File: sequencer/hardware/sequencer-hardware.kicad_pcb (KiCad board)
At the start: 4 copper layers, 111 parts, among them J1 Barrel Jack, J10 JST_4-pin_male, J11 Conn_01x03, J12 Conn_01x03, J13 Conn_01x03, J14 Conn_01x03, J15 JST_4-pin_male, J16 JST_4-pin_male, J17 Conn_01x03, J2 40Pin 0.1", J3 USB_B_Micro, J4 Conn_01x02_Male, J5 JST 4-Pin male, J6 TS Out, J7 Conn_01x03_Male, J8 Conn_01x03_Male, J9 JST_4-pin_male, SW2 SW_Push, SW3 SW_Push, U1 L7805_A, U2 L7805_D, U3 ICL7660, U4 NCP1117-3.3_TO252, U5 OPA703UA, U6 OPA703UA, U7 W25Q128JVS, U8 RP2040, Y1 12MHz 18pF

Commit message: More routing
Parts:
- moved R2 150.9 mm to (57.1, 135.5), turned to -90 degrees
- moved SW2 148.6 mm to (63.5, 133.3)
- moved R24 138.5 mm to (238.3, 24.1), turned to 0 degrees
- moved J10 130.8 mm to (222.2, 19.1), turned to -90 degrees
- moved R23 130.6 mm to (238.3, 20.3), turned to 0 degrees
- moved R1 129.1 mm to (76.6, 109.2)
- moved R22 127.7 mm to (232.8, 24.1), turned to 0 degrees
- moved R16 127.6 mm to (231.1, 130.4), turned to -90 degrees
- moved C20 122.5 mm to (228.6, 141.0), turned to 90 degrees
- moved R28 121.3 mm to (252.2, 60.5)
- moved R15 119.8 mm to (231.1, 117.7), turned to -90 degrees
- moved C22 119.5 mm to (231.1, 141.0), turned to 90 degrees
- moved R27 118.4 mm to (252.2, 65.2)
- moved C24 117.7 mm to (234.9, 140.6), turned to 90 degrees
- moved C26 116.3 mm to (237.5, 140.6), turned to 90 degrees
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
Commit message: Adjust component placement
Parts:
- added SW1: PWR, Connector_PinHeader_2.00mm:PinHeader_1x02_P2.00mm_Vertical, F.Cu at (49.9, 44.7)
- moved C28 186.6 mm to (76.7, 112.0)
- moved C29 186.6 mm to (76.7, 117.1)
- moved R27 186.6 mm to (72.9, 116.9)
- moved R29 186.6 mm to (69.1, 112.1)
- moved R30 186.6 mm to (69.1, 116.9)
- moved R28 179.5 mm to (78.0, 103.6)
- moved J15 176.0 mm to (71.8, 105.1)
- moved J17 168.3 mm to (64.4, 62.7), turned to -90 degrees
- moved R33 161.4 mm to (67.8, 81.0), turned to -90 degrees
- moved R23 160.6 mm to (83.4, 62.6), turned to 180 degrees
- moved C37 158.8 mm to (70.1, 145.8), turned to 90 degrees
- moved C36 158.7 mm to (72.6, 145.8), turned to 90 degrees
- moved C35 158.6 mm to (75.2, 145.8), turned to 90 degrees
- moved R34 158.1 mm to (68.6, 75.2), turned to -90 degrees
- moved R24 154.8 mm to (88.6, 63.5), turned to 180 degrees
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
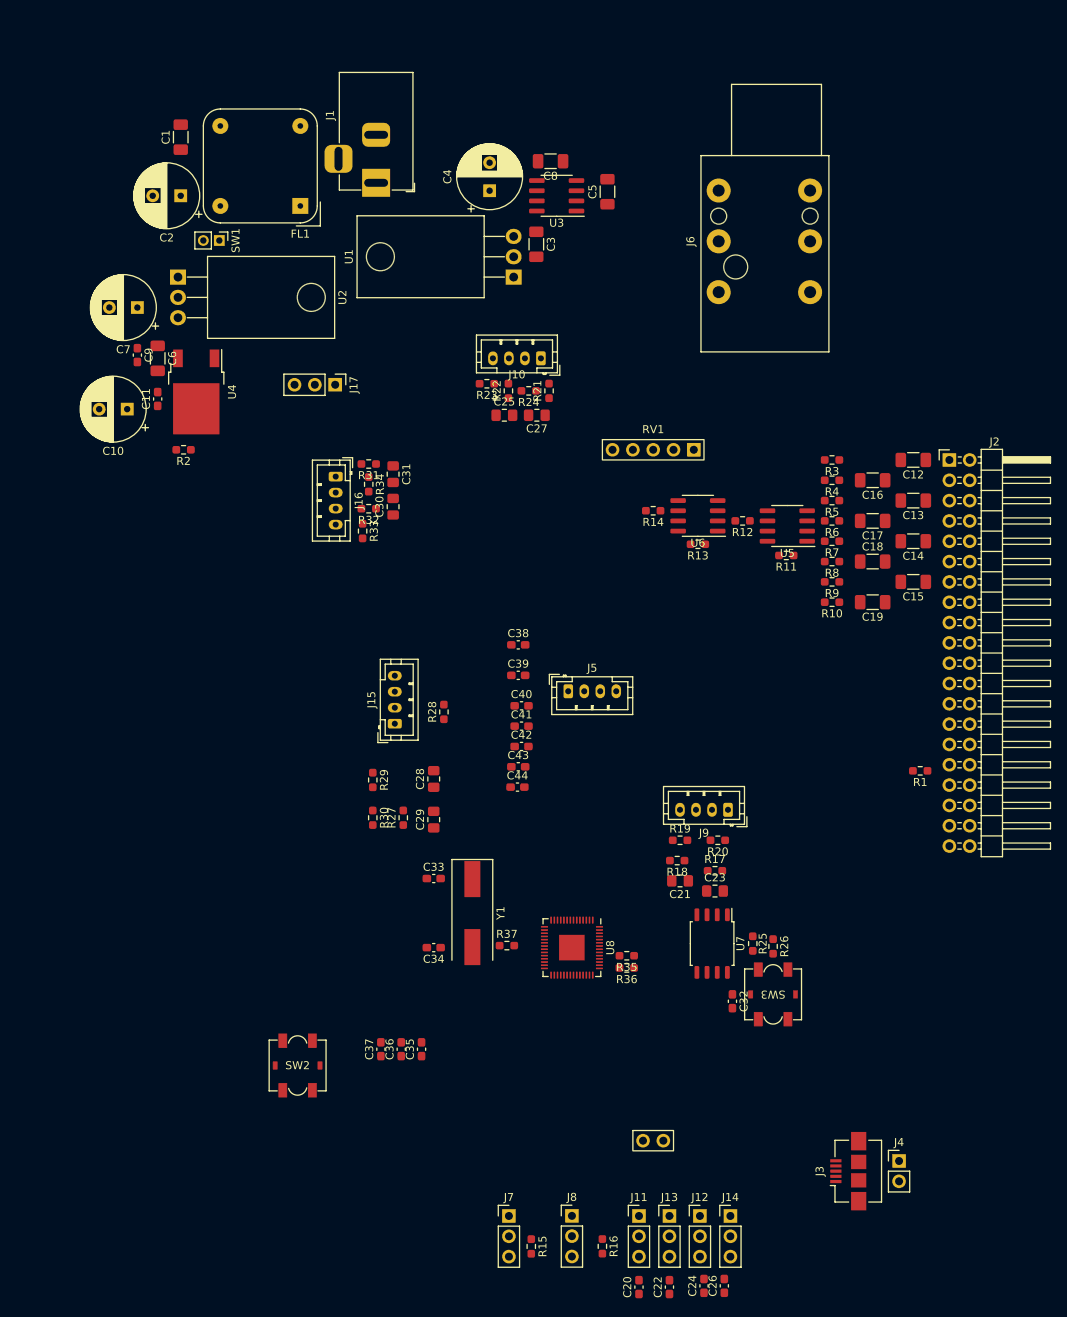
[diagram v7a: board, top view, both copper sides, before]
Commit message: add mounting holes, arrange all parts
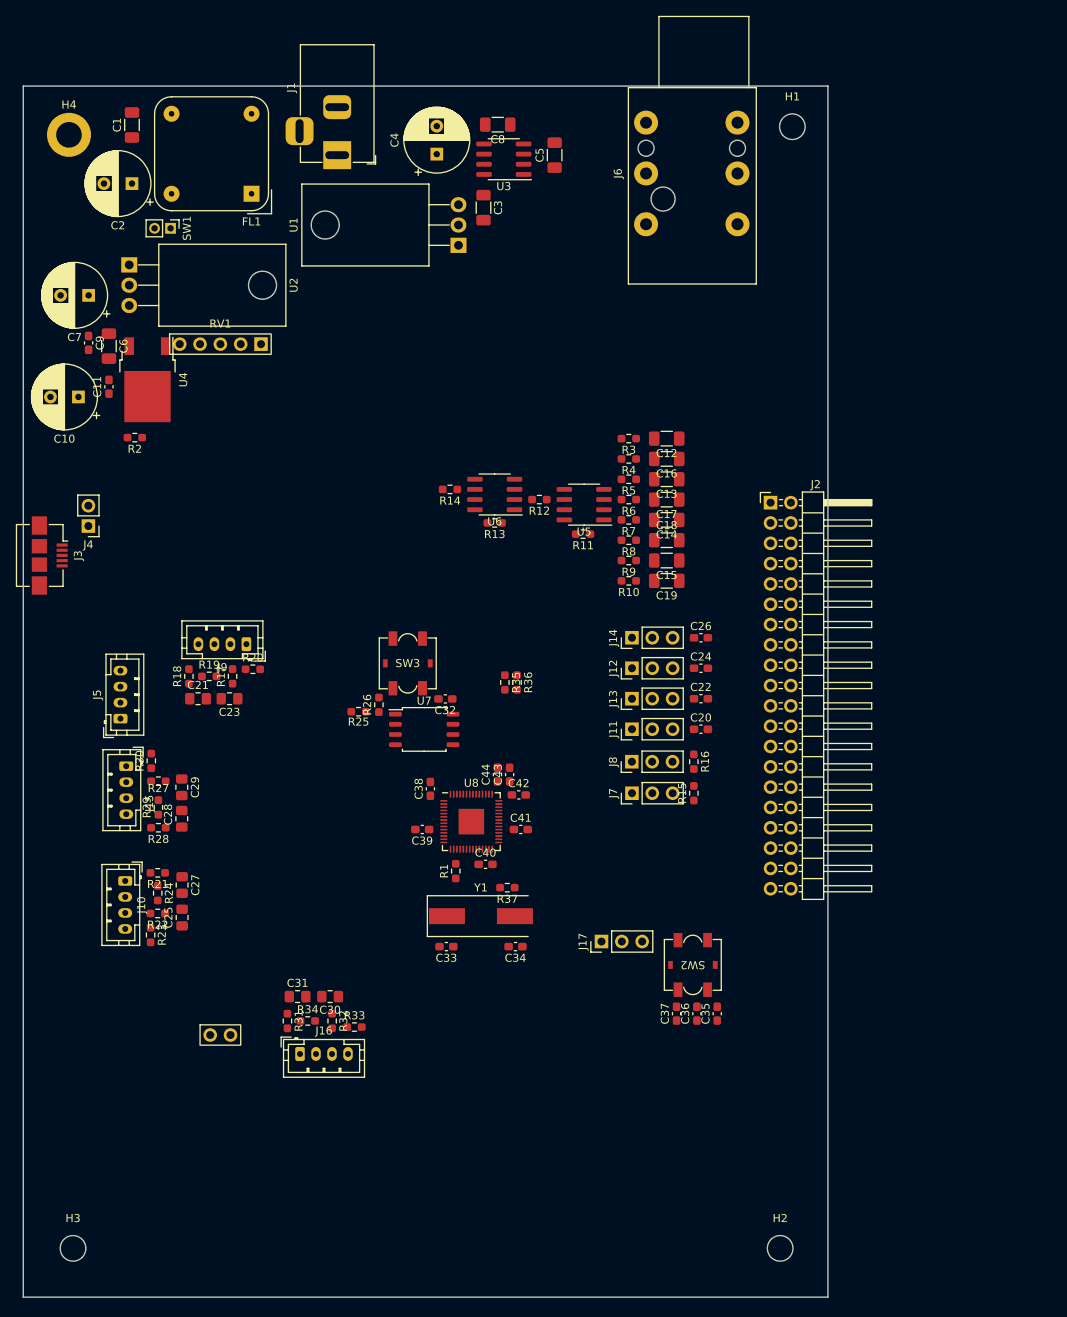
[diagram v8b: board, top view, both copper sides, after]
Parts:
- added H1: MountingHole, MountingHole:MountingHole_3.2mm_M3_ISO14580, F.Cu at (121.5, 30.5)
- added H2: MountingHole, MountingHole:MountingHole_3.2mm_M3_ISO14580, F.Cu at (120.0, 170.7)
- added H3: MountingHole, MountingHole:MountingHole_3.2mm_M3_ISO14580, F.Cu at (31.6, 170.7)
- added H4: MountingHole, MountingHole:MountingHole_3.2mm_M3_ISO14580_Pad, F.Cu at (31.1, 31.5)
- moved J4 128.7 mm to (33.5, 80.4), turned to 180 degrees
- moved J3 126.0 mm to (28.7, 84.1), turned to -90 degrees
- moved J10 83.5 mm to (38.1, 124.8), turned to -90 degrees
- moved C26 81.1 mm to (110.1, 94.4), turned to 0 degrees
- moved R23 80.7 mm to (41.3, 131.5), turned to -90 degrees
- moved R22 78.7 mm to (42.2, 128.8), turned to 180 degrees
- moved R24 78.1 mm to (42.2, 126.3), turned to -90 degrees
- moved R21 77.6 mm to (42.2, 123.7), turned to 180 degrees
- moved C24 77.2 mm to (110.1, 98.2), turned to 0 degrees
- moved J17 77.1 mm to (97.7, 132.3), turned to 90 degrees
- moved C25 74.6 mm to (45.3, 129.3), turned to 90 degrees
- moved C22 73.7 mm to (110.1, 102.0), turned to 0 degrees
- moved C27 73.6 mm to (45.3, 125.3), turned to -90 degrees
- moved J14 73.3 mm to (101.5, 94.4), turned to 90 degrees
- moved J16 72.3 mm to (60.0, 146.4), turned to 0 degrees
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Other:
- board outline added: 100.6 x 151.4 mm
